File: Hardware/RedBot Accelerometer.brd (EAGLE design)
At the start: 11.4 x 17.8 mm, 17 parts, among them U1 MMA8452Q, U2 MIC5205-3.3V

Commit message: Add some part info for BOM purposes.
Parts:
- renumbered U$1 to U3
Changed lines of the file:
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@@
 <grid distance="0.05" unitdist="inch" unit="inch" style="lines" multiple="1" display="yes" altdistance="0.005" altunitdist="inch" altunit="inch"/>
 <layers>
-<layer number="1" name="Top" color="4" fill="1" visible="no" active="yes"/>
+<layer number="1" name="Top" color="4" fill="1" visible="yes" active="yes"/>
 <layer number="2" name="Route2" color="1" fill="3" visible="no" active="yes"/>
 <layer number="15" name="Route15" color="4" fill="6" visible="no" active="yes"/>
@@
 <layer number="19" name="Unrouted" color="6" fill="1" visible="yes" active="yes"/>
 <layer number="20" name="Dimension" color="15" fill="1" visible="yes" active="yes"/>
-<layer number="21" name="tPlace" color="16" fill="1" visible="no" active="yes"/>
+<layer number="21" name="tPlace" color="16" fill="1" visible="yes" active="yes"/>
 <layer number="22" name="bPlace" color="14" fill="1" visible="yes" active="yes"/>
-<layer number="23" name="tOrigins" color="15" fill="1" visible="no" active="yes"/>
+<layer number="23" name="tOrigins" color="15" fill="1" visible="yes" active="yes"/>
 <layer number="24" name="bOrigins" color="15" fill="1" visible="yes" active="yes"/>
 <layer number="25" name="tNames" color="7" fill="1" visible="no" active="yes"/>
@@
 <layer number="42" name="bRestrict" color="1" fill="10" visible="no" active="yes"/>
 <layer number="44" name="Drills" color="7" fill="1" visible="no" active="yes"/>
-<layer number="45" name="Holes" color="7" fill="1" visible="no" active="yes"/>
+<layer number="45" name="Holes" color="7" fill="1" visible="yes" active="yes"/>
 <layer number="46" name="Milling" color="3" fill="1" visible="no" active="yes"/>
-<layer number="51" name="tDocu" color="6" fill="1" visible="no" active="yes"/>
+<layer number="51" name="tDocu" color="6" fill="1" visible="yes" active="yes"/>
 <layer number="52" name="bDocu" color="7" fill="1" visible="no" active="yes"/>
 <layer number="3" name="Route3" color="4" fill="3" visible="no" active="no"/>
@@
 <attribute name="PROD_ID" value="CAP-00810" x="45.72" y="-1.905" size="1.778" layer="27" display="off"/>
 </element>
-<element name="U$1" library="SparkFun-DigitalIC" package="PSOP-8" value="PCA9306" x="2.54" y="12.7" rot="R180"/>
-<element name="U1" library="SparkFun-Sensors" package="QFN-16_0.5MM" value="MMA8452Q" x="8.89" y="12.7" rot="R270"/>
+<element name="U3" library="SparkFun-DigitalIC" package="PSOP-8" value="PCA9306" x="2.54" y="12.7" rot="R180">
+<attribute name="PROD_ID" value="IC-10023" x="2.54" y="12.7" size="1.778" layer="27" rot="R180" display="off"/>
+</element>
+<element name="U1" library="SparkFun-Sensors" package="QFN-16_0.5MM" value="MMA8452Q" x="8.89" y="12.7" rot="R270">
+<attribute name="PROD_ID" value="IC-10769" x="8.89" y="12.7" size="1.778" layer="27" rot="R270" display="off"/>
+</element>
 <element name="R1" library="SparkFun-Resistors" package="0402-RES" value="10k" x="6.35" y="11.43" rot="R270">
 <attribute name="PROD_ID" value="RES-00824" x="-13.97" y="-11.43" size="1.778" layer="27" rot="R270" display="off"/>
@@
 <contactref element="C1" pad="2"/>
 <contactref element="U2" pad="2"/>
-<contactref element="U$1" pad="4"/>
+<contactref element="U3" pad="4"/>
 <contactref element="C4" pad="2"/>
 <contactref element="JP1" pad="5"/>
@@
 <contactref element="U2" pad="5"/>
 <contactref element="R1" pad="2"/>
-<contactref element="U$1" pad="1"/>
+<contactref element="U3" pad="1"/>
 <contactref element="R3" pad="2"/>
 <contactref element="R2" pad="2"/>
@@
 </signal>
 <signal name="N$2">
-<contactref element="U$1" pad="8"/>
+<contactref element="U3" pad="8"/>
 <contactref element="R6" pad="1"/>
-<contactref element="U$1" pad="7"/>
+<contactref element="U3" pad="7"/>
 <contactref element="C4" pad="1"/>
 <wire x1="0.635" y1="12.05" x2="2.428" y2="12.05" width="0.2032" layer="1"/>
@@
 </signal>
 <signal name="SCL">
-<contactref element="U$1" pad="6"/>
+<contactref element="U3" pad="6"/>
 <contactref element="R5" pad="1"/>
 <contactref element="JP1" pad="2"/>
@@
 </signal>
 <signal name="SDA">
-<contactref element="U$1" pad="5"/>
+<contactref element="U3" pad="5"/>
 <contactref element="R4" pad="1"/>
 <contactref element="JP1" pad="1"/>
@@
 </signal>
 <signal name="SCL1">
-<contactref element="U$1" pad="2"/>
+<contactref element="U3" pad="2"/>
 <contactref element="R3" pad="1"/>
 <contactref element="U1" pad="4"/>
@@
 </signal>
 <signal name="SDA1">
-<contactref element="U$1" pad="3"/>
+<contactref element="U3" pad="3"/>
 <contactref element="R2" pad="1"/>
 <contactref element="U1" pad="6"/>

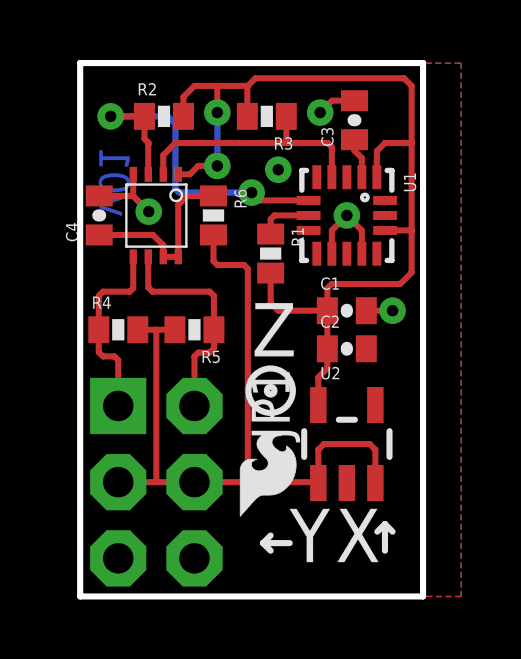
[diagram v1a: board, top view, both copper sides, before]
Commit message: Advance to rev 10 for release  - added pin numbers for alignment to top silk  - change revision numbers
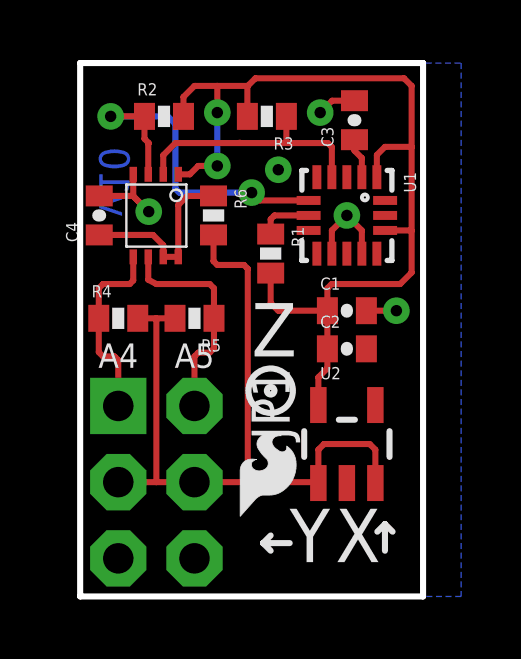
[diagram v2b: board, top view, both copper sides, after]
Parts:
- moved R4 0.38 mm to (1.27, 9.27)
- moved R5 0.38 mm to (3.81, 9.27)
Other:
- board text added: "A4"
- board text added: "A5"
- board text added: "M. Hord"
- board text added: "v10"
- board text removed: "v01"
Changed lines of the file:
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@@
 <text x="3.81" y="7.62" size="0.8128" layer="22" font="vector" ratio="15" rot="MR270" align="center-right">SCL</text>
 <text x="1.27" y="7.62" size="0.8128" layer="22" font="vector" ratio="15" rot="MR270" align="center-right">SDA</text>
-<text x="1.651" y="14.986" size="1.016" layer="16" font="vector" ratio="15" rot="MR270">v01</text>
+<text x="1.651" y="14.986" size="1.016" layer="16" font="vector" ratio="15" rot="MR270">v10</text>
+<text x="-46.99" y="1.27" size="1.778" layer="27" font="vector" ratio="15">M. Hord</text>
+<text x="1.27" y="7.62" size="0.8128" layer="21" font="vector" ratio="15" align="bottom-center">A4</text>
+<text x="3.81" y="7.62" size="0.8128" layer="21" font="vector" ratio="15" align="bottom-center">A5</text>
 </plain>
 <attributes>
@@
 <attribute name="PROD_ID" value="RES-07856" x="-24.257" y="36.322" size="1.778" layer="27" rot="R180" display="off"/>
 </element>
-<element name="R4" library="SparkFun-Resistors" package="0402-RES" value="1k" x="1.27" y="8.89">
-<attribute name="PROD_ID" value="RES-07856" x="35.56" y="-11.43" size="1.778" layer="27" display="off"/>
-</element>
-<element name="R5" library="SparkFun-Resistors" package="0402-RES" value="1k" x="3.81" y="8.89" rot="R180">
-<attribute name="PROD_ID" value="RES-07856" x="-34.29" y="29.21" size="1.778" layer="27" rot="R180" display="off"/>
+<element name="R4" library="SparkFun-Resistors" package="0402-RES" value="1k" x="1.27" y="9.271">
+<attribute name="PROD_ID" value="RES-07856" x="35.56" y="-11.049" size="1.778" layer="27" display="off"/>
+</element>
+<element name="R5" library="SparkFun-Resistors" package="0402-RES" value="1k" x="3.81" y="9.271" rot="R180">
+<attribute name="PROD_ID" value="RES-07856" x="-34.29" y="29.591" size="1.778" layer="27" rot="R180" display="off"/>
 </element>
 <element name="U2" library="SparkFun-PowerIC" package="SOT23-5" value="MIC5205-3.3V" x="8.89" y="5.08">
@@
 <polygon width="0.2032" layer="1" isolate="0.3048">
 <vertex x="0" y="17.78"/>
-<vertex x="12.7" y="17.78"/>
-<vertex x="12.7" y="0"/>
+<vertex x="11.43" y="17.78"/>
+<vertex x="11.43" y="0"/>
 <vertex x="0" y="0"/>
 </polygon>
@@
 <wire x1="0.635" y1="13.35" x2="1.763" y2="13.35" width="0.2032" layer="1"/>
 <wire x1="1.763" y1="13.35" x2="2.286" y2="12.827" width="0.2032" layer="1"/>
-<wire x1="9.54" y1="9.525" x2="10.414" y2="9.525" width="0.2032" layer="1"/>
-<via x="10.414" y="9.525" extent="1-16" drill="0.381"/>
+<wire x1="9.54" y1="9.525" x2="10.541" y2="9.525" width="0.2032" layer="1"/>
+<via x="10.541" y="9.525" extent="1-16" drill="0.381"/>
 <wire x1="9.39" y1="11.425" x2="9.39" y2="12.2" width="0.2032" layer="1"/>
 <wire x1="9.39" y1="12.2" x2="8.89" y2="12.7" width="0.2032" layer="1"/>
@@
 <wire x1="10.668" y1="10.414" x2="11.049" y2="10.795" width="0.2032" layer="1"/>
 <wire x1="10.165" y1="12.2" x2="11.041" y2="12.2" width="0.2032" layer="1"/>
-<wire x1="9.89" y1="13.975" x2="9.89" y2="14.843" width="0.2032" layer="1"/>
-<wire x1="9.89" y1="14.843" x2="10.16" y2="15.113" width="0.2032" layer="1"/>
-<wire x1="11.049" y1="17.018" x2="11.049" y2="15.113" width="0.2032" layer="1"/>
-<wire x1="11.049" y1="15.113" x2="11.049" y2="12.192" width="0.2032" layer="1"/>
+<wire x1="9.89" y1="13.975" x2="9.89" y2="14.716" width="0.2032" layer="1"/>
+<wire x1="9.89" y1="14.716" x2="10.16" y2="14.986" width="0.2032" layer="1"/>
+<wire x1="11.049" y1="17.018" x2="11.049" y2="14.986" width="0.2032" layer="1"/>
+<wire x1="11.049" y1="14.986" x2="11.049" y2="12.192" width="0.2032" layer="1"/>
 <wire x1="11.049" y1="12.192" x2="11.049" y2="10.795" width="0.2032" layer="1"/>
 <wire x1="11.041" y1="12.2" x2="11.049" y2="12.192" width="0.2032" layer="1"/>
@@
 <wire x1="10.795" y1="17.272" x2="5.842" y2="17.272" width="0.2032" layer="1"/>
 <wire x1="5.842" y1="17.272" x2="5.588" y2="17.018" width="0.2032" layer="1"/>
-<wire x1="10.16" y1="15.113" x2="11.049" y2="15.113" width="0.2032" layer="1"/>
+<wire x1="10.16" y1="14.986" x2="11.049" y2="14.986" width="0.2032" layer="1"/>
 </signal>
 <signal name="5V">
@@
 <contactref element="JP1" pad="3"/>
 <contactref element="JP1" pad="4"/>
-<wire x1="1.92" y1="8.89" x2="2.54" y2="8.89" width="0.2032" layer="1"/>
-<wire x1="2.54" y1="8.89" x2="3.16" y2="8.89" width="0.2032" layer="1"/>
-<wire x1="2.54" y1="8.89" x2="2.54" y2="3.81" width="0.2032" layer="1"/>
+<wire x1="1.92" y1="9.271" x2="2.54" y2="9.271" width="0.2032" layer="1"/>
+<wire x1="2.54" y1="9.271" x2="3.16" y2="9.271" width="0.2032" layer="1"/>
+<wire x1="2.54" y1="9.271" x2="2.54" y2="3.81" width="0.2032" layer="1"/>
 <wire x1="2.54" y1="3.81" x2="1.27" y2="3.81" width="0.2032" layer="1"/>
 <wire x1="2.54" y1="3.81" x2="3.81" y2="3.81" width="0.2032" layer="1"/>
@@
 <contactref element="R5" pad="1"/>
 <contactref element="JP1" pad="2"/>
-<wire x1="2.27" y1="11.32" x2="2.27" y2="10.303" width="0.2032" layer="1"/>
-<wire x1="2.27" y1="10.303" x2="2.413" y2="10.16" width="0.2032" layer="1"/>
-<wire x1="2.413" y1="10.16" x2="4.318" y2="10.16" width="0.2032" layer="1"/>
-<wire x1="4.318" y1="10.16" x2="4.46" y2="10.018" width="0.2032" layer="1"/>
-<wire x1="4.46" y1="8.89" x2="4.46" y2="10.018" width="0.2032" layer="1"/>
-<wire x1="4.46" y1="8.89" x2="4.46" y2="8.27" width="0.2032" layer="1"/>
+<wire x1="2.27" y1="11.32" x2="2.27" y2="10.557" width="0.2032" layer="1"/>
+<wire x1="2.27" y1="10.557" x2="2.54" y2="10.414" width="0.2032" layer="1"/>
+<wire x1="2.54" y1="10.414" x2="4.318" y2="10.414" width="0.2032" layer="1"/>
+<wire x1="4.318" y1="10.414" x2="4.46" y2="10.272" width="0.2032" layer="1"/>
+<wire x1="4.46" y1="9.271" x2="4.46" y2="10.272" width="0.2032" layer="1"/>
+<wire x1="4.46" y1="9.271" x2="4.46" y2="8.27" width="0.2032" layer="1"/>
 <wire x1="4.46" y1="8.27" x2="4.318" y2="8.128" width="0.2032" layer="1"/>
 <wire x1="4.318" y1="8.128" x2="3.937" y2="8.128" width="0.2032" layer="1"/>
@@
 <contactref element="R4" pad="1"/>
 <contactref element="JP1" pad="1"/>
-<wire x1="1.77" y1="11.32" x2="1.77" y2="10.279" width="0.2032" layer="1"/>
-<wire x1="1.77" y1="10.279" x2="1.651" y2="10.16" width="0.2032" layer="1"/>
-<wire x1="1.651" y1="10.16" x2="0.762" y2="10.16" width="0.2032" layer="1"/>
-<wire x1="0.762" y1="10.16" x2="0.62" y2="10.018" width="0.2032" layer="1"/>
-<wire x1="0.62" y1="8.89" x2="0.62" y2="10.018" width="0.2032" layer="1"/>
-<wire x1="0.62" y1="8.89" x2="0.62" y2="8.143" width="0.2032" layer="1"/>
+<wire x1="1.77" y1="11.32" x2="1.77" y2="10.533" width="0.2032" layer="1"/>
+<wire x1="1.77" y1="10.533" x2="1.651" y2="10.414" width="0.2032" layer="1"/>
+<wire x1="1.651" y1="10.414" x2="0.762" y2="10.414" width="0.2032" layer="1"/>
+<wire x1="0.762" y1="10.414" x2="0.62" y2="10.272" width="0.2032" layer="1"/>
+<wire x1="0.62" y1="9.271" x2="0.62" y2="10.272" width="0.2032" layer="1"/>
+<wire x1="0.62" y1="9.271" x2="0.62" y2="8.143" width="0.2032" layer="1"/>
 <wire x1="0.62" y1="8.143" x2="0.762" y2="8.001" width="0.2032" layer="1"/>
 <wire x1="0.762" y1="8.001" x2="1.143" y2="8.001" width="0.2032" layer="1"/>
@@
 </signal>
 </signals>
+<errors>
+</errors>
 </board>
 </drawing>

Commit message: Production readied
added fiducial references & created panel for manufacture
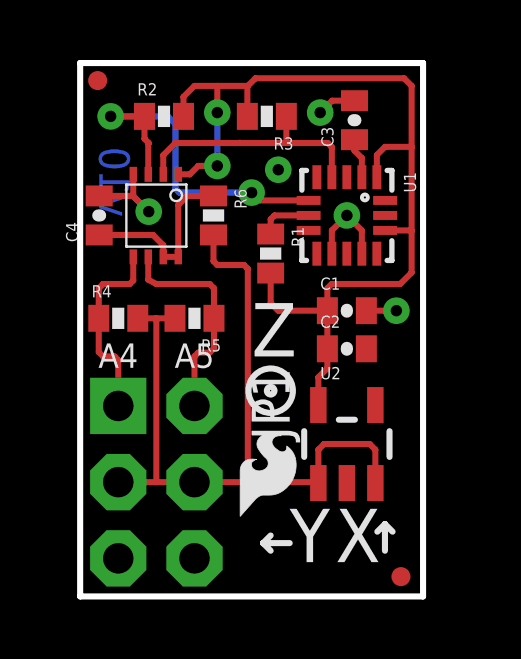
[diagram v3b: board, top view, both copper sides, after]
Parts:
- added FID1, FID2: FIDUCIALUFIDUCIAL, SparkFun-Aesthetics:MICRO-FIDUCIAL
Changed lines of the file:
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@@
 <setting verticaltext="up"/>
 </settings>
-<grid distance="0.05" unitdist="inch" unit="inch" style="lines" multiple="1" display="yes" altdistance="0.005" altunitdist="inch" altunit="inch"/>
+<grid distance="0.001" unitdist="inch" unit="inch" style="lines" multiple="1" display="yes" altdistance="0.01" altunitdist="inch" altunit="inch"/>
 <layers>
 <layer number="1" name="Top" color="4" fill="1" visible="yes" active="yes"/>
-<layer number="2" name="Route2" color="1" fill="3" visible="no" active="yes"/>
-<layer number="15" name="Route15" color="4" fill="6" visible="no" active="yes"/>
+<layer number="2" name="Route2" color="1" fill="3" visible="yes" active="yes"/>
+<layer number="15" name="Route15" color="4" fill="6" visible="yes" active="yes"/>
 <layer number="16" name="Bottom" color="1" fill="1" visible="yes" active="yes"/>
 <layer number="17" name="Pads" color="2" fill="1" visible="yes" active="yes"/>
 <layer number="18" name="Vias" color="2" fill="1" visible="yes" active="yes"/>
 <layer number="19" name="Unrouted" color="6" fill="1" visible="yes" active="yes"/>
-<layer number="20" name="Dimension" color="15" fill="1" visible="yes" active="yes"/>
-<layer number="21" name="tPlace" color="16" fill="1" visible="yes" active="yes"/>
-<layer number="22" name="bPlace" color="14" fill="1" visible="yes" active="yes"/>
+<layer number="20" name="Dimension" color="6" fill="1" visible="yes" active="yes"/>
+<layer number="21" name="tPlace" color="6" fill="1" visible="yes" active="yes"/>
+<layer number="22" name="bPlace" color="6" fill="1" visible="yes" active="yes"/>
 <layer number="23" name="tOrigins" color="15" fill="1" visible="yes" active="yes"/>
 <layer number="24" name="bOrigins" color="15" fill="1" visible="yes" active="yes"/>
-<layer number="25" name="tNames" color="7" fill="1" visible="no" active="yes"/>
-<layer number="26" name="bNames" color="7" fill="1" visible="no" active="yes"/>
-<layer number="27" name="tValues" color="7" fill="1" visible="no" active="yes"/>
-<layer number="28" name="bValues" color="7" fill="1" visible="no" active="yes"/>
-<layer number="29" name="tStop" color="7" fill="3" visible="no" active="yes"/>
-<layer number="30" name="bStop" color="7" fill="6" visible="no" active="yes"/>
-<layer number="31" name="tCream" color="7" fill="4" visible="no" active="yes"/>
-<layer number="32" name="bCream" color="7" fill="5" visible="no" active="yes"/>
-<layer number="39" name="tKeepout" color="4" fill="11" visible="no" active="yes"/>
-<layer number="40" name="bKeepout" color="1" fill="11" visible="no" active="yes"/>
-<layer number="41" name="tRestrict" color="4" fill="10" visible="no" active="yes"/>
-<layer number="42" name="bRestrict" color="1" fill="10" visible="no" active="yes"/>
-<layer number="44" name="Drills" color="7" fill="1" visible="no" active="yes"/>
+<layer number="25" name="tNames" color="7" fill="1" visible="yes" active="yes"/>
+<layer number="26" name="bNames" color="7" fill="1" visible="yes" active="yes"/>
+<layer number="27" name="tValues" color="7" fill="1" visible="yes" active="yes"/>
+<layer number="28" name="bValues" color="7" fill="1" visible="yes" active="yes"/>
+<layer number="29" name="tStop" color="7" fill="3" visible="yes" active="yes"/>
+<layer number="30" name="bStop" color="7" fill="6" visible="yes" active="yes"/>
+<layer number="31" name="tCream" color="7" fill="4" visible="yes" active="yes"/>
+<layer number="32" name="bCream" color="7" fill="5" visible="yes" active="yes"/>
+<layer number="39" name="tKeepout" color="4" fill="11" visible="yes" active="yes"/>
+<layer number="40" name="bKeepout" color="1" fill="11" visible="yes" active="yes"/>
+<layer number="41" name="tRestrict" color="4" fill="10" visible="yes" active="yes"/>
+<layer number="42" name="bRestrict" color="1" fill="10" visible="yes" active="yes"/>
+<layer number="44" name="Drills" color="7" fill="1" visible="yes" active="yes"/>
 <layer number="45" name="Holes" color="7" fill="1" visible="yes" active="yes"/>
-<layer number="46" name="Milling" color="3" fill="1" visible="no" active="yes"/>
+<layer number="46" name="Milling" color="3" fill="1" visible="yes" active="yes"/>
 <layer number="51" name="tDocu" color="6" fill="1" visible="yes" active="yes"/>
-<layer number="52" name="bDocu" color="7" fill="1" visible="no" active="yes"/>
+<layer number="52" name="bDocu" color="7" fill="1" visible="yes" active="yes"/>
 <layer number="3" name="Route3" color="4" fill="3" visible="no" active="no"/>
 <layer number="4" name="Route4" color="1" fill="4" visible="no" active="no"/>
@@
 </element>
 <element name="JP1" library="SparkFun-Connectors" package="2X3-NS" value="" x="2.54" y="3.81" rot="R270"/>
+<element name="FID1" library="SparkFun-Aesthetics" package="MICRO-FIDUCIAL" value="FIDUCIALUFIDUCIAL" x="0.5842" y="17.1958"/>
+<element name="FID2" library="SparkFun-Aesthetics" package="MICRO-FIDUCIAL" value="FIDUCIALUFIDUCIAL" x="10.6934" y="0.6604"/>
 </elements>
 <signals>
@@
 <polygon width="0.2032" layer="16" isolate="0.3048">
 <vertex x="0" y="17.78"/>
-<vertex x="12.7" y="17.78"/>
-<vertex x="12.7" y="0"/>
+<vertex x="11.43" y="17.78"/>
+<vertex x="11.43" y="0"/>
 <vertex x="0" y="0"/>
 </polygon>
@@
 </signal>
 </signals>
-<errors>
-</errors>
 </board>
 </drawing>
